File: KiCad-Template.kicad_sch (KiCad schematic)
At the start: 1 part, among them U1 ESP32-S3-WROOM-1

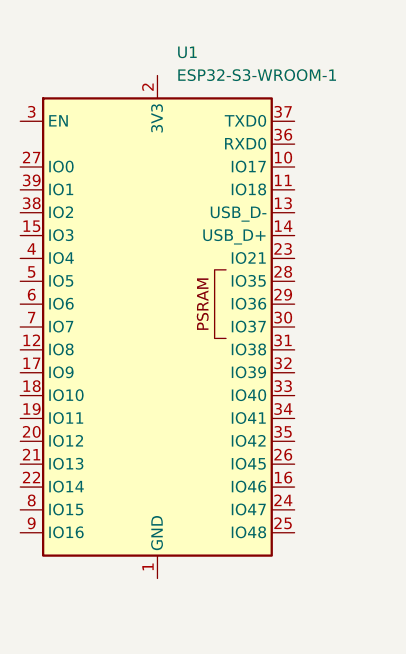
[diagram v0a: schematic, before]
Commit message: Add PWR and GND Net Classes
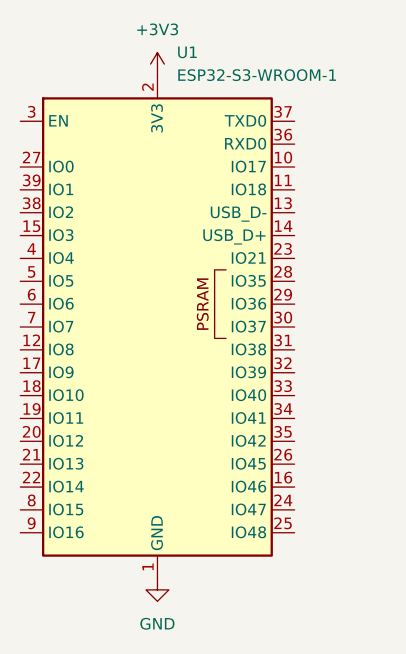
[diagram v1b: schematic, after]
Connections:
- net GND: now reaches U1.1 (GND), U1.40 (GND), U1.41 (GND)
- net +3V3: now reaches U1.2 (3V3)
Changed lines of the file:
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@@
 	(paper "A4")
+	(symbol
+		(lib_id "power:+3V3")
+		(at 144.78 78.74 0)
+		(unit 1)
+		(exclude_from_sim no)
+		(in_bom yes)
+		(on_board yes)
+		(dnp no)
+		(fields_autoplaced yes)
+		(property "Reference" "#PWR01"
+			(at 144.78 82.55 0)
+			(effects
+				(font
+					(size 1.27 1.27)
+				)
+				(hide yes)
+			)
+		)
+		(property "Value" "+3V3"
+			(at 144.78 73.66 0)
+			(effects
+				(font
+					(size 1.27 1.27)
+				)
+			)
+		)
+		(property "Footprint" ""
+			(at 144.78 78.74 0)
+			(effects
+				(font
+					(size 1.27 1.27)
+				)
+				(hide yes)
+			)
+		)
+		(property "Datasheet" ""
+			(at 144.78 78.74 0)
+			(effects
+				(font
+					(size 1.27 1.27)
+				)
+				(hide yes)
+			)
+		)
+		(property "Description" "Power symbol creates a global label with name \"+3V3\""
+			(at 144.78 78.74 0)
+			(effects
+				(font
+					(size 1.27 1.27)
+				)
+				(hide yes)
+			)
+		)
+		(pin "1"
+		)
+		(instances
+			(project ""
+				(path "/a7d0bfc3-312e-4bbd-9285-17fc6d48996f"
+					(reference "#PWR01")
+					(unit 1)
+				)
+			)
+		)
+	)
+	(symbol
+		(lib_id "power:GND")
+		(at 144.78 134.62 0)
+		(unit 1)
+		(exclude_from_sim no)
+		(in_bom yes)
+		(on_board yes)
+		(dnp no)
+		(fields_autoplaced yes)
+		(property "Reference" "#PWR02"
+			(at 144.78 140.97 0)
+			(effects
+				(font
+					(size 1.27 1.27)
+				)
+				(hide yes)
+			)
+		)
+		(property "Value" "GND"
+			(at 144.78 139.7 0)
+			(effects
+				(font
+					(size 1.27 1.27)
+				)
+			)
+		)
+		(property "Footprint" ""
+			(at 144.78 134.62 0)
+			(effects
+				(font
+					(size 1.27 1.27)
+				)
+				(hide yes)
+			)
+		)
+		(property "Datasheet" ""
+			(at 144.78 134.62 0)
+			(effects
+				(font
+					(size 1.27 1.27)
+				)
+				(hide yes)
+			)
+		)
+		(property "Description" "Power symbol creates a global label with name \"GND\" , ground"
+			(at 144.78 134.62 0)
+			(effects
+				(font
+					(size 1.27 1.27)
+				)
+				(hide yes)
+			)
+		)
+		(pin "1"
+		)
+		(instances
+			(project ""
+				(path "/a7d0bfc3-312e-4bbd-9285-17fc6d48996f"
+					(reference "#PWR02")
+					(unit 1)
+				)
+			)
+		)
+	)
 	(symbol
 		(lib_id "Custom:ESP32-S3-WROOM-1")
